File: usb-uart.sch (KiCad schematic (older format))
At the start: 16 parts, among them P5 USB-C-2.0-FEMALE, U3 FT230XS

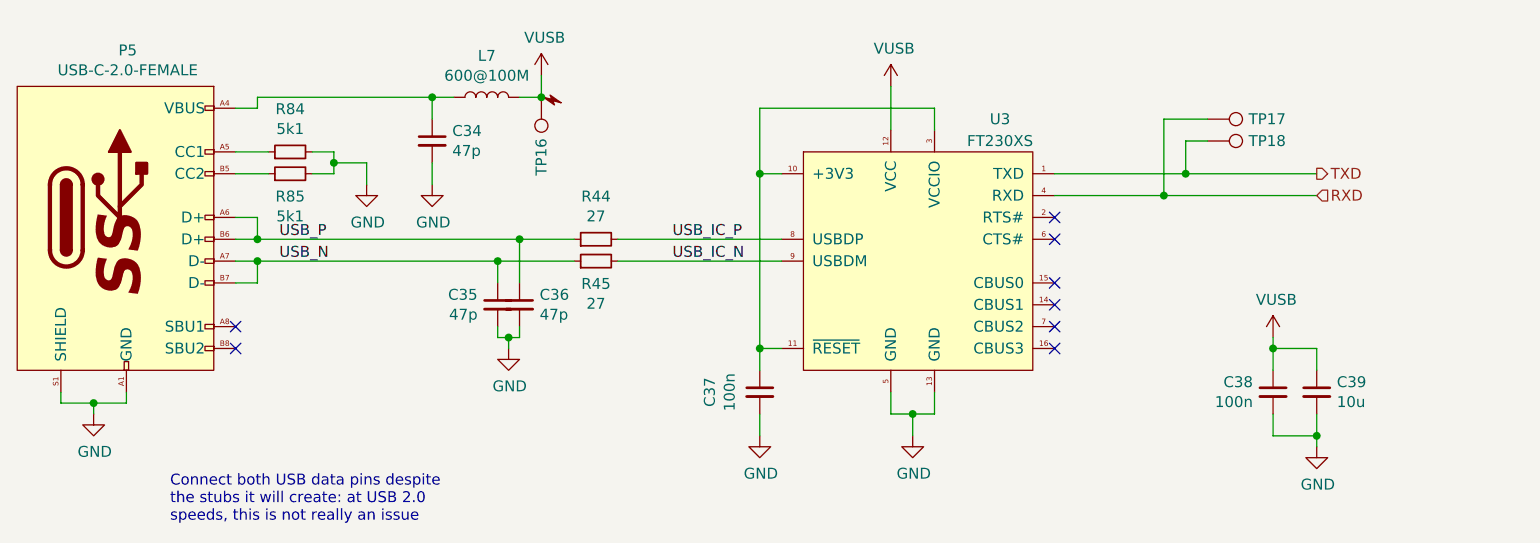
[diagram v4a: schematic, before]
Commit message: sch, pcb: Replace USB-C connectors with vertical ones
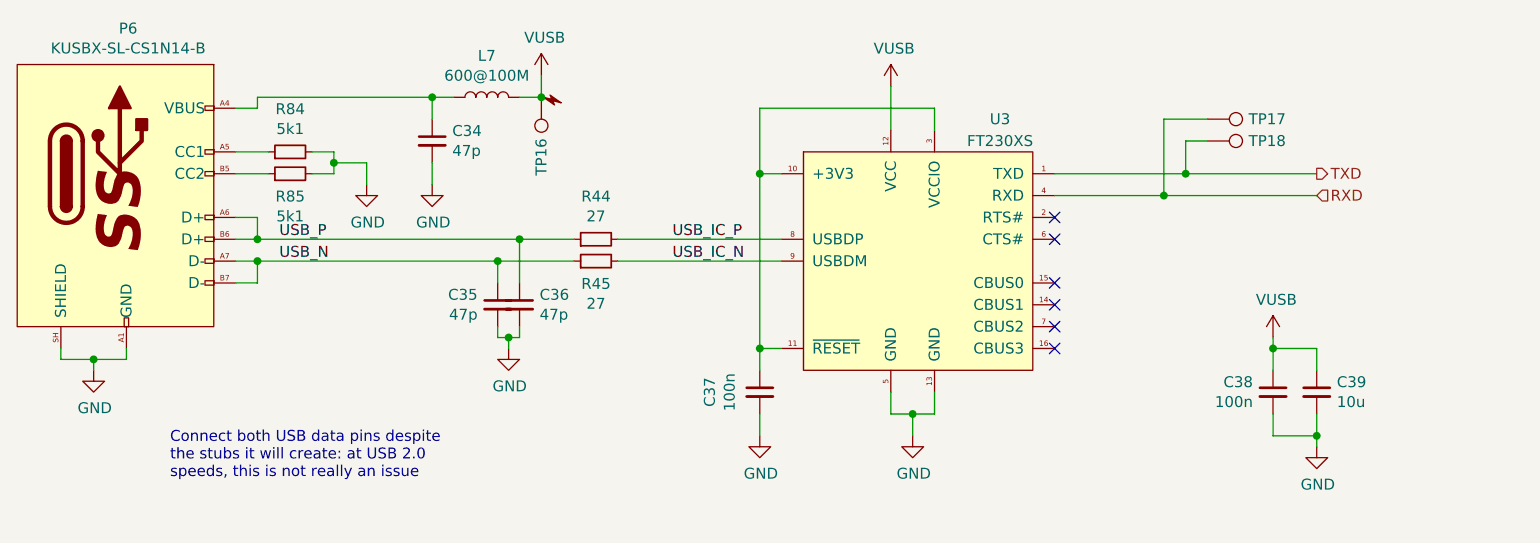
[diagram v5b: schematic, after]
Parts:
- removed P5: USB-C-2.0-FEMALE, pimouss-motherboard:USB-C-FEMALE, symbol pimouss-motherboard:USB-C-2.0-FEMALE
- added P6: KUSBX-SL-CS1N14-B, pimouss-motherboard:KUSBX-SL-CS1N14-B, symbol pimouss-motherboard:KUSBX-SL-CS1N14-B
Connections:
- net GND: now also P6.A1 (GND), P6.A12 (GND), P6.B1 (GND), P6.B12 (GND), P6.SH (SHIELD)
- net USB_N: now also P6.A7 (D-), P6.B7 (D-)
- net USB_P: now also P6.A6 (D+), P6.B6 (D+)
- net at C34.1, L7.1: now also P6.A4 (VBUS), P6.A9 (VBUS), P6.B4 (VBUS), P6.B9 (VBUS)
- net at R84.1: now also P6.A5 (CC1)
- net at R85.1: now also P6.B5 (CC2)
- no-connect marks 8 -> 6
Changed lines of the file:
@@
 Comment4 ""
 $EndDescr
-$Comp
-L pimouss-motherboard:USB-C-2.0-FEMALE P5
-U 1 1 5D27BBAF
-P 2800 3100
-F 0 "P5" H 3306 3265 50  0000 C CNN
-F 1 "USB-C-2.0-FEMALE" H 3306 3174 50  0000 C CNN
-F 2 "pimouss-motherboard:USB-C-FEMALE" H 3550 1600 50  0001 C CNN
-F 3 "https://www.usb.org/sites/default/files/documents/usb_type-c.zip" H 3450 2600 50  0001 C CNN
-	1    2800 3100
-	1    0    0    -1
-$EndComp
 Wire Wire Line
 	5550 3800 6300 3800
@@
 Text Label 4000 3900 0    50   ~ 0
 USB_N
-NoConn ~ 3800 4200
-NoConn ~ 3800 4300
 Wire Wire Line
 	5100 4000 5100 3800
@@
 	5100 4200 5100 4250
 Wire Wire Line
-	3300 4500 3300 4550
-Wire Wire Line
-	3000 4550 3000 4500
+	3300 4300 3300 4350
+Wire Wire Line
+	3000 4350 3000 4300
 $Comp
 L Device:L L?
@@
 	7550 3500 8150 3500
 Wire Wire Line
-	3000 4550 3150 4550
+	3000 4350 3150 4350
 $Comp
 L power:GND #PWR080
 U 1 1 5D29968A
-P 3150 4600
-F 0 "#PWR080" H 3150 4350 50  0001 C CNN
-F 1 "GND" H 3155 4427 50  0000 C CNN
-F 2 "" H 3150 4600 50  0001 C CNN
-F 3 "" H 3150 4600 50  0001 C CNN
-	1    3150 4600
-	1    0    0    -1
-$EndComp
-Wire Wire Line
-	3150 4600 3150 4550
-Connection ~ 3150 4550
-Wire Wire Line
-	3150 4550 3300 4550
-Text Notes 3500 5100 0    50   ~ 0
+P 3150 4400
+F 0 "#PWR080" H 3150 4150 50  0001 C CNN
+F 1 "GND" H 3155 4227 50  0000 C CNN
+F 2 "" H 3150 4400 50  0001 C CNN
+F 3 "" H 3150 4400 50  0001 C CNN
+	1    3150 4400
+	1    0    0    -1
+$EndComp
+Wire Wire Line
+	3150 4400 3150 4350
+Connection ~ 3150 4350
+Wire Wire Line
+	3150 4350 3300 4350
+Text Notes 3500 4900 0    50   ~ 0
 Connect both USB data pins despite\nthe stubs it will create: at USB 2.0\nspeeds, this is not really an issue
 $Comp
@@
 	1    0    0    -1
 $EndComp
+$Comp
+L pimouss-motherboard:KUSBX-SL-CS1N14-B P6
+U 1 1 5DF126C5
+P 2800 3000
+F 0 "P6" H 3308 3165 50  0000 C CNN
+F 1 "KUSBX-SL-CS1N14-B" H 3308 3074 50  0000 C CNN
+F 2 "pimouss-motherboard:KUSBX-SL-CS1N14-B" H 3550 1600 50  0001 C CNN
+F 3 "https://www.usb.org/sites/default/files/documents/usb_type-c.zip" H 3450 2600 50  0001 C CNN
+	1    2800 3000
+	1    0    0    -1
+$EndComp
